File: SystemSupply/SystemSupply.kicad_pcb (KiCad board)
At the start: 2 copper layers, 75 x 75 mm, 45 parts, among them J1 Conn_01x01, J10 Screw_Terminal_01x02, J2 Conn_01x01, J3 4P4C, J4 Conn_01x01, J5 Conn_01x01, J6 Screw_Terminal_01x02, J7 4P4C, J8 Screw_Terminal_01x02, J9 Screw_Terminal_01x02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

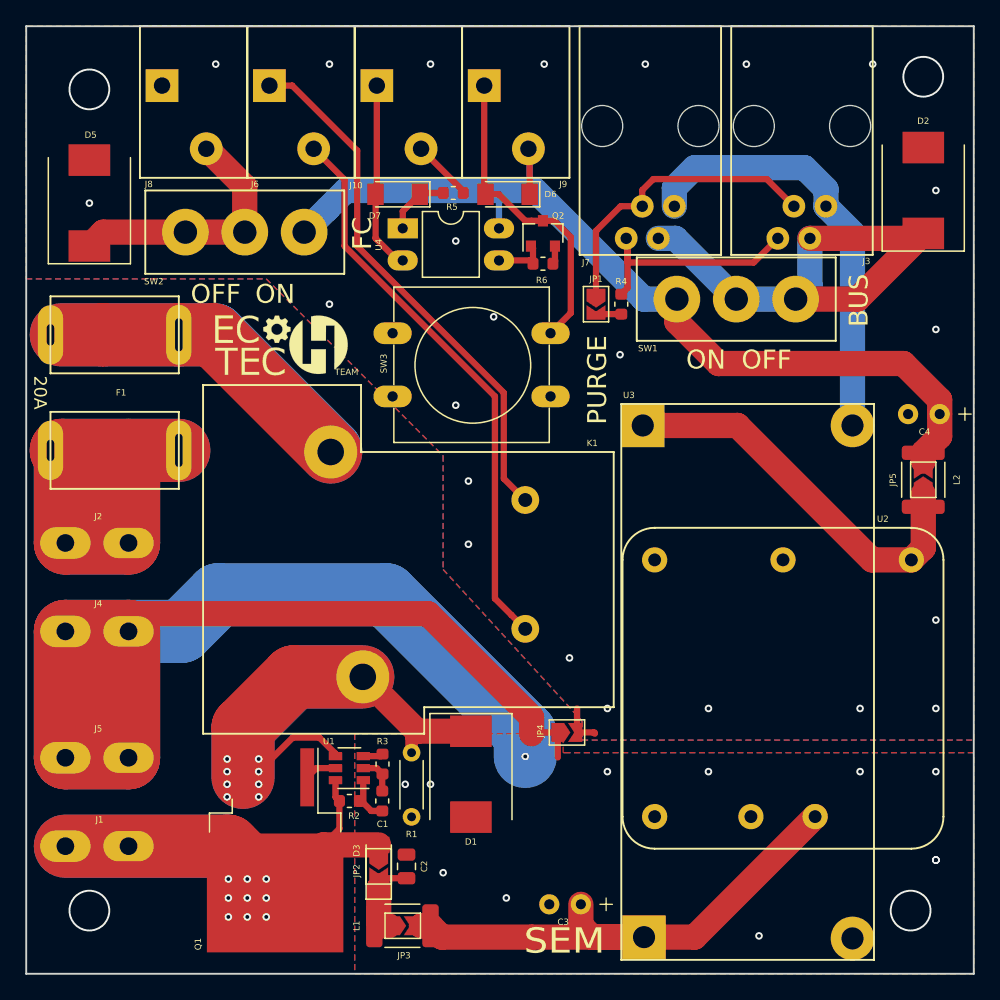
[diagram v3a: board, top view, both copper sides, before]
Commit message: Removed Switches from bus devices and added mounting holes in schematics.
Squashed commit of the following:

commit 448b4f84a5f64686dc4334a0b6d81609891ca7cf
Author: Paweł <mackipawel@gmail.com>
Date:   Sun Apr 28 20:22:14 2019 +0200

    Added mouting holes to SystemSupply.

commit d45917b7024ecbe087cb8328a2c33d3ab10399ff
Author: Paweł <mackipawel@gmail.com>
Date:   Sun Apr 28 20:13:41 2019 +0200

    Added mouting holes to SafetySystem.

commit 6365380671305e2241dc821ec3b00ae08a997ac5
Author: Paweł <mackipawel@gmail.com>
Date:   Sun Apr 28 20:11:13 2019 +0200

    Added mouting holes to SafetySupply.

commit 00163d4bba61eb48f9ebb4c601b04017e78006be
Author: Paweł <mackipawel@gmail.com>
Date:   Sun Apr 28 20:06:38 2019 +0200

    Fixed MotorController.

commit ec0507ca51ef80aebbe2605505e7109beac59e98
Author: Paweł <mackipawel@gmail.com>
Date:   Sun Apr 28 19:54:40 2019 +0200

    Fixed MotorDriver.
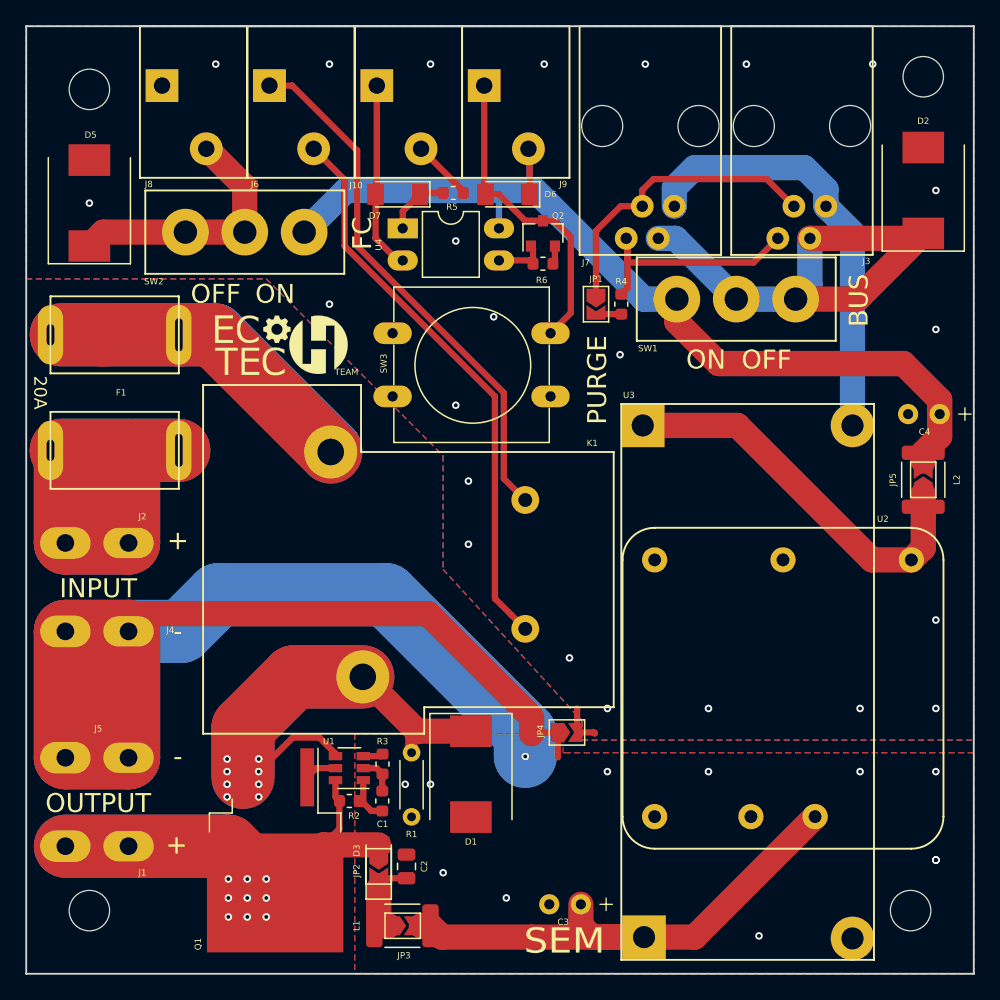
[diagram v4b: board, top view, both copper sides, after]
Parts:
- added H1: MountingHole, MountingHole:MountingHole_3.2mm_M3, F.Cu at (130.0, 160.0)
- added H2: MountingHole, MountingHole:MountingHole_3.2mm_M3, F.Cu at (65.0, 95.0)
- added H3: MountingHole, MountingHole:MountingHole_3.2mm_M3, F.Cu at (131.0, 94.0)
- added H4: MountingHole, MountingHole:MountingHole_3.2mm_M3, F.Cu at (65.0, 160.0)
- G1: renamed from G***; value LOGO -> EcoTechLogo
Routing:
- net (no net): vias 4 -> 0
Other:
- board text added: "+"
- board text added: "-"
- board text added: "INPUT"
- board text added: "OUTPUT"
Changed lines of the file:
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@@
   (general
     (thickness 1.6)
-    (drawings 13)
-    (tracks 262)
+    (drawings 19)
+    (tracks 258)
     (zones 0)
-    (modules 45)
+    (modules 49)
     (nets 28)
   )
@@
     (add_net "Net-(U3-Pad6)")
   )
+  (module MountingHole:MountingHole_3.2mm_M3 (layer F.Cu)
+    (at 130 160)
+    (descr "Mounting Hole 3.2mm, no annular, M3")
+    (tags "mounting hole 3.2mm no annular m3")
+    (attr virtual)
+    (fp_text reference H1 (at 0 -4.2) (layer F.SilkS) hide
+      (effects (font (size 1 1) (thickness 0.15)))
+    )
+    (fp_text value MountingHole (at 0 4.2) (layer F.Fab)
+      (effects (font (size 1 1) (thickness 0.15)))
+    )
+    (fp_circle (center 0 0) (end 3.45 0) (layer F.CrtYd) (width 0.05))
+    (fp_circle (center 0 0) (end 3.2 0) (layer Cmts.User) (width 0.15))
+    (fp_text user %R (at 0.3 0) (layer F.Fab)
+      (effects (font (size 1 1) (thickness 0.15)))
+    )
+    (pad 1 np_thru_hole circle (at 0 0) (size 3.2 3.2) (drill 3.2) (layers *.Cu *.Mask))
+  )
+  (module MountingHole:MountingHole_3.2mm_M3 (layer F.Cu)
+    (at 131 94)
+    (descr "Mounting Hole 3.2mm, no annular, M3")
+    (tags "mounting hole 3.2mm no annular m3")
+    (attr virtual)
+    (fp_text reference H3 (at 0 -4.2) (layer F.SilkS) hide
+      (effects (font (size 1 1) (thickness 0.15)))
+    )
+    (fp_text value MountingHole (at 0 4.2) (layer F.Fab)
+      (effects (font (size 1 1) (thickness 0.15)))
+    )
+    (fp_text user %R (at 0.3 0) (layer F.Fab)
+      (effects (font (size 1 1) (thickness 0.15)))
+    )
+    (fp_circle (center 0 0) (end 3.2 0) (layer Cmts.User) (width 0.15))
+    (fp_circle (center 0 0) (end 3.45 0) (layer F.CrtYd) (width 0.05))
+    (pad 1 np_thru_hole circle (at 0 0) (size 3.2 3.2) (drill 3.2) (layers *.Cu *.Mask))
+  )
+  (module MountingHole:MountingHole_3.2mm_M3 (layer F.Cu)
+    (at 65 160)
+    (descr "Mounting Hole 3.2mm, no annular, M3")
+    (tags "mounting hole 3.2mm no annular m3")
+    (attr virtual)
+    (fp_text reference H4 (at 0 -4.2) (layer F.SilkS) hide
+      (effects (font (size 1 1) (thickness 0.15)))
+    )
+    (fp_text value MountingHole (at 0 4.2) (layer F.Fab)
+      (effects (font (size 1 1) (thickness 0.15)))
+    )
+    (fp_circle (center 0 0) (end 3.45 0) (layer F.CrtYd) (width 0.05))
+    (fp_circle (center 0 0) (end 3.2 0) (layer Cmts.User) (width 0.15))
+    (fp_text user %R (at 0.3 0) (layer F.Fab)
+      (effects (font (size 1 1) (thickness 0.15)))
+    )
+    (pad 1 np_thru_hole circle (at 0 0) (size 3.2 3.2) (drill 3.2) (layers *.Cu *.Mask))
+  )
+  (module MountingHole:MountingHole_3.2mm_M3 (layer F.Cu)
+    (at 65 95)
+    (descr "Mounting Hole 3.2mm, no annular, M3")
+    (tags "mounting hole 3.2mm no annular m3")
+    (attr virtual)
+    (fp_text reference H2 (at 0 -4.2) (layer F.SilkS) hide
+      (effects (font (size 1 1) (thickness 0.15)))
+    )
+    (fp_text value MountingHole (at 0 4.2) (layer F.Fab)
+      (effects (font (size 1 1) (thickness 0.15)))
+    )
+    (fp_text user %R (at 0.3 0) (layer F.Fab)
+      (effects (font (size 1 1) (thickness 0.15)))
+    )
+    (fp_circle (center 0 0) (end 3.2 0) (layer Cmts.User) (width 0.15))
+    (fp_circle (center 0 0) (end 3.45 0) (layer F.CrtYd) (width 0.05))
+    (pad 1 np_thru_hole circle (at 0 0) (size 3.2 3.2) (drill 3.2) (layers *.Cu *.Mask))
+  )
   (module Footprints:C_Radial_D6.3mm_H11.0mm_P2.50mm (layer F.Cu)
     (at 103.9 159.5 180)
@@
   (module Footprints:FlatConnector_63 (layer F.Cu)
     (at 63.1 137.9 90)
-    (fp_text reference J4 (at 2.2 2.6) (layer F.SilkS)
+    (fp_text reference J4 (at 0.1 8.3) (layer F.SilkS)
       (effects (font (size 0.5 0.5) (thickness 0.1)))
     )
@@
   (module Footprints:FlatConnector_63 (layer F.Cu)
     (at 63.1 130.9 90)
-    (fp_text reference J2 (at 2.1 2.6) (layer F.SilkS)
+    (fp_text reference J2 (at 2.1 6.1) (layer F.SilkS)
       (effects (font (size 0.5 0.5) (thickness 0.1)))
     )
@@
   (module Footprints:FlatConnector_63 (layer F.Cu)
     (at 63.1 154.9 90)
-    (fp_text reference J1 (at 2.1 2.7) (layer F.SilkS)
+    (fp_text reference J1 (at -2.1 6.1) (layer F.SilkS)
       (effects (font (size 0.5 0.5) (thickness 0.1)))
     )
@@
   (module Footprints:EcoTech (layer F.Cu)
     (at 80.3 115.5)
-    (fp_text reference G*** (at 0 0) (layer F.SilkS) hide
+    (fp_text reference G1 (at 0 0) (layer F.SilkS) hide
       (effects (font (size 1.524 1.524) (thickness 0.3)))
     )
-    (fp_text value LOGO (at 0.75 0) (layer F.SilkS) hide
+    (fp_text value EcoTechLogo (at 0.75 0) (layer F.SilkS) hide
       (effects (font (size 1.524 1.524) (thickness 0.3)))
     )
@@
       (xy -0.594643 -0.074098) (xy -0.47301 -0.071399)) (layer F.SilkS) (width 0.01))
   )
+  (gr_text + (at 72 130.7) (layer F.SilkS)
+    (effects (font (size 1.5 1.5) (thickness 0.25)))
+  )
+  (gr_text + (at 71.9 154.8) (layer F.SilkS)
+    (effects (font (size 1.5 1.5) (thickness 0.25)))
+  )
+  (gr_text - (at 72 147.8) (layer F.SilkS)
+    (effects (font (size 1.5 1.5) (thickness 0.25)))
+  )
+  (gr_text - (at 72 137.9) (layer F.SilkS)
+    (effects (font (size 1.5 1.5) (thickness 0.25)))
+  )
+  (gr_text OUTPUT (at 65.7 151.5) (layer F.SilkS)
+    (effects (font (size 1.5 1.5) (thickness 0.25)))
+  )
+  (gr_text INPUT (at 65.7 134.5) (layer F.SilkS)
+    (effects (font (size 1.5 1.5) (thickness 0.25)))
+  )
   (gr_text SEM (at 102.6 162.4) (layer F.SilkS)
     (effects (font (size 2 2.2) (thickness 0.25)))
@@
   (gr_line (start 60 165) (end 135 165) (layer Edge.Cuts) (width 0.15))
   (gr_line (start 60 90) (end 60 165) (layer Edge.Cuts) (width 0.15))
-  (via (at 65 160) (size 3.3) (drill 3) (layers F.Cu B.Cu) (net 0))
-  (via (at 130 160) (size 3.3) (drill 3) (layers F.Cu B.Cu) (net 0))
-  (via (at 131 94) (size 3.3) (drill 3) (layers F.Cu B.Cu) (net 0))
-  (via (at 65 95) (size 3.3) (drill 3) (layers F.Cu B.Cu) (net 0))
   (via (at 75.9 148) (size 0.6) (drill 0.3) (layers F.Cu B.Cu) (net 1))
   (via (at 75.9 151) (size 0.6) (drill 0.3) (layers F.Cu B.Cu) (net 1))

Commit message: Added testpoints.
Squashed commit of the following:

commit b78741095f1293168643ce5f943c13a7eb09b318
Author: Paweł <mackipawel@gmail.com>
Date:   Thu May 2 10:22:35 2019 +0200

    Added testpoints to remaining projects.

commit d708f3fd02ddff10684a41533d76b9b66ea6c8f4
Author: Paweł <mackipawel@gmail.com>
Date:   Sun Apr 28 23:49:47 2019 +0200

    Added testpoints in MotorController and MotorDriver.
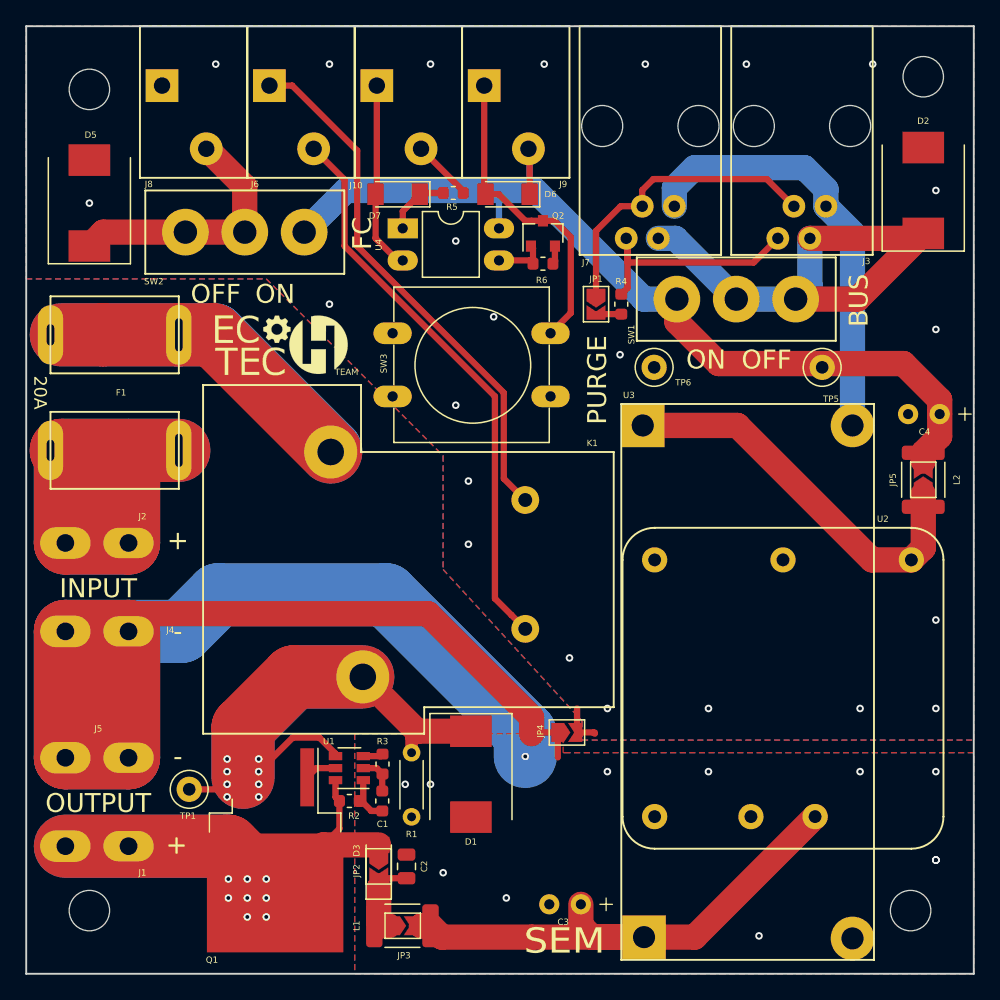
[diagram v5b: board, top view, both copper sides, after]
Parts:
- added TP1: TestPoint, TestPoint:TestPoint_Loop_D1.80mm_Drill1.0mm_Beaded, F.Cu at (72.9, 150.4)
- added TP5: TestPoint, TestPoint:TestPoint_Loop_D1.80mm_Drill1.0mm_Beaded, F.Cu at (123.0, 117.0)
- added TP6: TestPoint, TestPoint:TestPoint_Loop_D1.80mm_Drill1.0mm_Beaded, F.Cu at (109.7, 117.0)
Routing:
- net Net-(D1-Pad1): track 58.1 -> 61.7 mm
- net +24V: vias 9 -> 8
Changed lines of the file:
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@@
     (thickness 1.6)
     (drawings 19)
-    (tracks 258)
+    (tracks 259)
     (zones 0)
-    (modules 49)
+    (modules 52)
     (nets 28)
   )
@@
   )
   (setup
-    (last_trace_width 0.25)
+    (last_trace_width 0.5)
     (user_trace_width 0.3)
     (user_trace_width 0.5)
@@
     (add_net "Net-(U3-Pad6)")
   )
+  (module TestPoint:TestPoint_Loop_D1.80mm_Drill1.0mm_Beaded (layer F.Cu)
+    (at 72.9 150.4)
+    (descr "wire loop with bead as test point, loop diameter 1.8mm, hole diameter 1.0mm")
+    (tags "test point wire loop bead")
+    (fp_text reference TP1 (at -0.1 2.1) (layer F.SilkS)
+      (effects (font (size 0.5 0.5) (thickness 0.1)))
+    )
+    (fp_text value TestPoint (at 0 -2.8) (layer F.Fab)
+      (effects (font (size 1 1) (thickness 0.15)))
+    )
+    (fp_text user %R (at 0.7 2.5) (layer F.Fab)
+      (effects (font (size 1 1) (thickness 0.15)))
+    )
+    (fp_circle (center 0 0) (end 1.3 0) (layer F.Fab) (width 0.12))
+    (fp_line (start -0.9 0.2) (end -0.9 -0.2) (layer F.Fab) (width 0.12))
+    (fp_line (start 0.9 0.2) (end -0.9 0.2) (layer F.Fab) (width 0.12))
+    (fp_line (start 0.9 -0.2) (end 0.9 0.2) (layer F.Fab) (width 0.12))
+    (fp_line (start -0.9 -0.2) (end 0.9 -0.2) (layer F.Fab) (width 0.12))
+    (fp_circle (center 0 0) (end 1.5 0) (layer F.SilkS) (width 0.12))
+    (fp_circle (center 0 0) (end 1.8 0) (layer F.CrtYd) (width 0.05))
+    (pad 1 thru_hole circle (at 0 0) (size 2 2) (drill 1) (layers *.Cu *.Mask)
+      (net 1 "Net-(D1-Pad1)"))
+    (model ${KISYS3DMOD}/TestPoint.3dshapes/TestPoint_Loop_D1.80mm_Drill1.0mm_Beaded.wrl
+      (at (xyz 0 0 0))
+      (scale (xyz 1 1 1))
+      (rotate (xyz 0 0 0))
+    )
+  )
+  (module TestPoint:TestPoint_Loop_D1.80mm_Drill1.0mm_Beaded (layer F.Cu)
+    (at 123 117)
+    (descr "wire loop with bead as test point, loop diameter 1.8mm, hole diameter 1.0mm")
+    (tags "test point wire loop bead")
+    (fp_text reference TP5 (at 0.7 2.5) (layer F.SilkS)
+      (effects (font (size 0.5 0.5) (thickness 0.1)))
+    )
+    (fp_text value TestPoint (at 0 -2.8) (layer F.Fab)
+      (effects (font (size 1 1) (thickness 0.15)))
+    )
+    (fp_text user %R (at 0.7 2.5) (layer F.Fab)
+      (effects (font (size 1 1) (thickness 0.15)))
+    )
+    (fp_circle (center 0 0) (end 1.3 0) (layer F.Fab) (width 0.12))
+    (fp_line (start -0.9 0.2) (end -0.9 -0.2) (layer F.Fab) (width 0.12))
+    (fp_line (start 0.9 0.2) (end -0.9 0.2) (layer F.Fab) (width 0.12))
+    (fp_line (start 0.9 -0.2) (end 0.9 0.2) (layer F.Fab) (width 0.12))
+    (fp_line (start -0.9 -0.2) (end 0.9 -0.2) (layer F.Fab) (width 0.12))
+    (fp_circle (center 0 0) (end 1.5 0) (layer F.SilkS) (width 0.12))
+    (fp_circle (center 0 0) (end 1.8 0) (layer F.CrtYd) (width 0.05))
+    (pad 1 thru_hole circle (at 0 0) (size 2 2) (drill 1) (layers *.Cu *.Mask)
+      (net 15 +12V))
+    (model ${KISYS3DMOD}/TestPoint.3dshapes/TestPoint_Loop_D1.80mm_Drill1.0mm_Beaded.wrl
+      (at (xyz 0 0 0))
+      (scale (xyz 1 1 1))
+      (rotate (xyz 0 0 0))
+    )
+  )
+  (module TestPoint:TestPoint_Loop_D1.80mm_Drill1.0mm_Beaded (layer F.Cu)
+    (at 109.7 117)
+    (descr "wire loop with bead as test point, loop diameter 1.8mm, hole diameter 1.0mm")
+    (tags "test point wire loop bead")
+    (fp_text reference TP6 (at 2.3 1.2) (layer F.SilkS)
+      (effects (font (size 0.5 0.5) (thickness 0.1)))
+    )
+    (fp_text value TestPoint (at 0 -2.8) (layer F.Fab)
+      (effects (font (size 1 1) (thickness 0.15)))
+    )
+    (fp_circle (center 0 0) (end 1.8 0) (layer F.CrtYd) (width 0.05))
+    (fp_circle (center 0 0) (end 1.5 0) (layer F.SilkS) (width 0.12))
+    (fp_line (start -0.9 -0.2) (end 0.9 -0.2) (layer F.Fab) (width 0.12))
+    (fp_line (start 0.9 -0.2) (end 0.9 0.2) (layer F.Fab) (width 0.12))
+    (fp_line (start 0.9 0.2) (end -0.9 0.2) (layer F.Fab) (width 0.12))
+    (fp_line (start -0.9 0.2) (end -0.9 -0.2) (layer F.Fab) (width 0.12))
+    (fp_circle (center 0 0) (end 1.3 0) (layer F.Fab) (width 0.12))
+    (fp_text user %R (at 0.7 2.5) (layer F.Fab)
+      (effects (font (size 1 1) (thickness 0.15)))
+    )
+    (pad 1 thru_hole circle (at 0 0) (size 2 2) (drill 1) (layers *.Cu *.Mask)
+      (net 4 GND))
+    (model ${KISYS3DMOD}/TestPoint.3dshapes/TestPoint_Loop_D1.80mm_Drill1.0mm_Beaded.wrl
+      (at (xyz 0 0 0))
+      (scale (xyz 1 1 1))
+      (rotate (xyz 0 0 0))
+    )
+  )
   (module MountingHole:MountingHole_3.2mm_M3 (layer F.Cu)
     (at 130 160)
@@
     (attr virtual)
     (fp_text reference H1 (at 0 -4.2) (layer F.SilkS) hide
-      (effects (font (size 1 1) (thickness 0.15)))
+      (effects (font (size 0.5 0.5) (thickness 0.1)))
     )
     (fp_text value MountingHole (at 0 4.2) (layer F.Fab)
@@
     (attr virtual)
     (fp_text reference H3 (at 0 -4.2) (layer F.SilkS) hide
-      (effects (font (size 1 1) (thickness 0.15)))
+      (effects (font (size 0.5 0.5) (thickness 0.1)))
     )
     (fp_text value MountingHole (at 0 4.2) (layer F.Fab)
@@
     (attr virtual)
     (fp_text reference H4 (at 0 -4.2) (layer F.SilkS) hide
-      (effects (font (size 1 1) (thickness 0.15)))
+      (effects (font (size 0.5 0.5) (thickness 0.1)))
     )
     (fp_text value MountingHole (at 0 4.2) (layer F.Fab)
@@
     (attr virtual)
     (fp_text reference H2 (at 0 -4.2) (layer F.SilkS) hide
-      (effects (font (size 1 1) (thickness 0.15)))
+      (effects (font (size 0.5 0.5) (thickness 0.1)))
     )
     (fp_text value MountingHole (at 0 4.2) (layer F.Fab)
@@
   (module Footprints:5MS1S102AM2QE (layer F.Cu)
     (at 116.2 111.6)
-    (fp_text reference SW1 (at -7 3.9) (layer F.SilkS)
+    (fp_text reference SW1 (at -8.3 2.8 90) (layer F.SilkS)
       (effects (font (size 0.5 0.5) (thickness 0.1)))
     )
@@
     (tags "D2PAK DDPAK TO-263 D2PAK-3 TO-263-3 SOT-404")
     (attr smd)
-    (fp_text reference Q1 (at 7.425 6.1 270) (layer F.SilkS)
+    (fp_text reference Q1 (at 8.675 5) (layer F.SilkS)
       (effects (font (size 0.5 0.5) (thickness 0.1)))
     )
@@
     (at 80.3 115.5)
     (fp_text reference G1 (at 0 0) (layer F.SilkS) hide
-      (effects (font (size 1.524 1.524) (thickness 0.3)))
+      (effects (font (size 0.5 0.5) (thickness 0.1)))
     )
     (fp_text value EcoTechLogo (at 0.75 0) (layer F.SilkS) hide
@@
   (segment (start 90.5 146.24) (end 90.94 145.8) (width 1) (layer F.Cu) (net 1))
   (segment (start 90.5 147.5) (end 90.5 146.24) (width 1) (layer F.Cu) (net 1))
+  (segment (start 75.5 150.4) (end 75.9 150) (width 0.5) (layer F.Cu) (net 1))
+  (segment (start 72.4 150.4) (end 75.5 150.4) (width 0.5) (layer F.Cu) (net 1))
   (segment (start 63.1 147.9) (end 63.1 137.9) (width 5) (layer F.Cu) (net 2))
   (segment (start 68.1 137.9) (end 68.1 147.9) (width 5) (layer F.Cu) (net 2))
@@
   (via (at 77.5 159) (size 0.6) (drill 0.3) (layers F.Cu B.Cu) (net 6))
   (via (at 79 160.5) (size 0.6) (drill 0.3) (layers F.Cu B.Cu) (net 6))
-  (via (at 76 160.5) (size 0.6) (drill 0.3) (layers F.Cu B.Cu) (net 6))
   (segment (start 78.6 157.5) (end 77.5 160.5) (width 5) (layer F.Cu) (net 6))
   (segment (start 83.5 154.8) (end 79.7 158.6) (width 2) (layer F.Cu) (net 6))
